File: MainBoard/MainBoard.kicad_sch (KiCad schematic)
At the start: 53 parts, among them J1 Conn_02x04_Odd_Even, SW1 DSHP02TSGET, U1 W25Q16JVUXIQ, U13 74LVC1G34GW,125, U14 SIP32431DR3-T1GE3, U2 RP2040, Y1 12.000MHz

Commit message: Move main PCB into subdirectory so that we can add a bezel PCB to this repo
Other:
- company: Framework Computer Inc -> C. Scott Ananian
- title: LED Matrix Input Module -> Seven Segment Display Input Module
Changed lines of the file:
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@@
 	(paper "A3")
 	(title_block
-		(title "LED Matrix Input Module")
-		(date "2022-12-18")
-		(company "Framework Computer Inc")
+		(title "Seven Segment Display Input Module")
+		(date "2024-07-13")
+		(company "C. Scott Ananian")
 		(comment 1 "This work is licensed under a Creative Commons Attribution 4.0 International License")
-		(comment 2 "https://github.com/FrameworkComputer/InputModules")
-		(comment 3 "https://frame.work")
+		(comment 2 "https://github.com/cscott/SevenSegmentInputModule")
+		(comment 3 "https://cscott.net")
 	)
 	(junction
@@
 		)
 		(instances
-			(project "SevenSegment"
+			(project "MainBoard"
 				(path "/2fa7b4ce-e682-4c2e-9419-b1318fe8c56d"
 					(page "2")

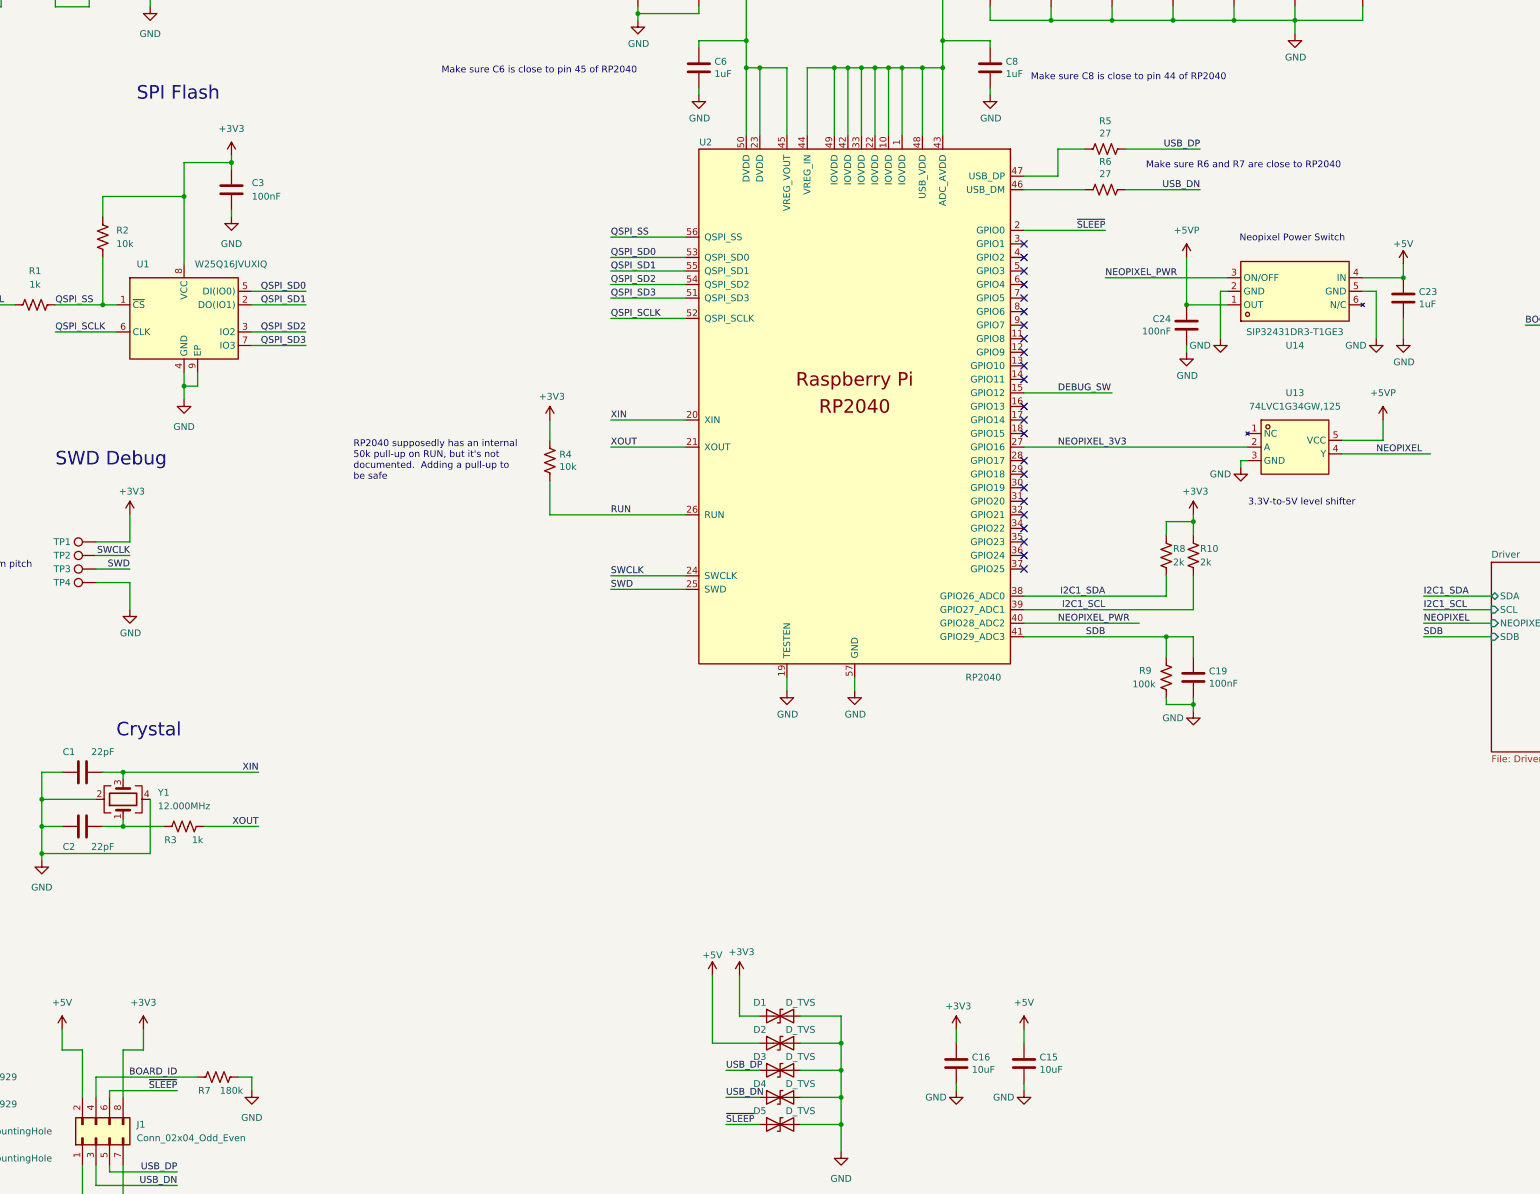
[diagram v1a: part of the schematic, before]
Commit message: Optimize for manufacturability (use JLCPCB basic parts, etc)
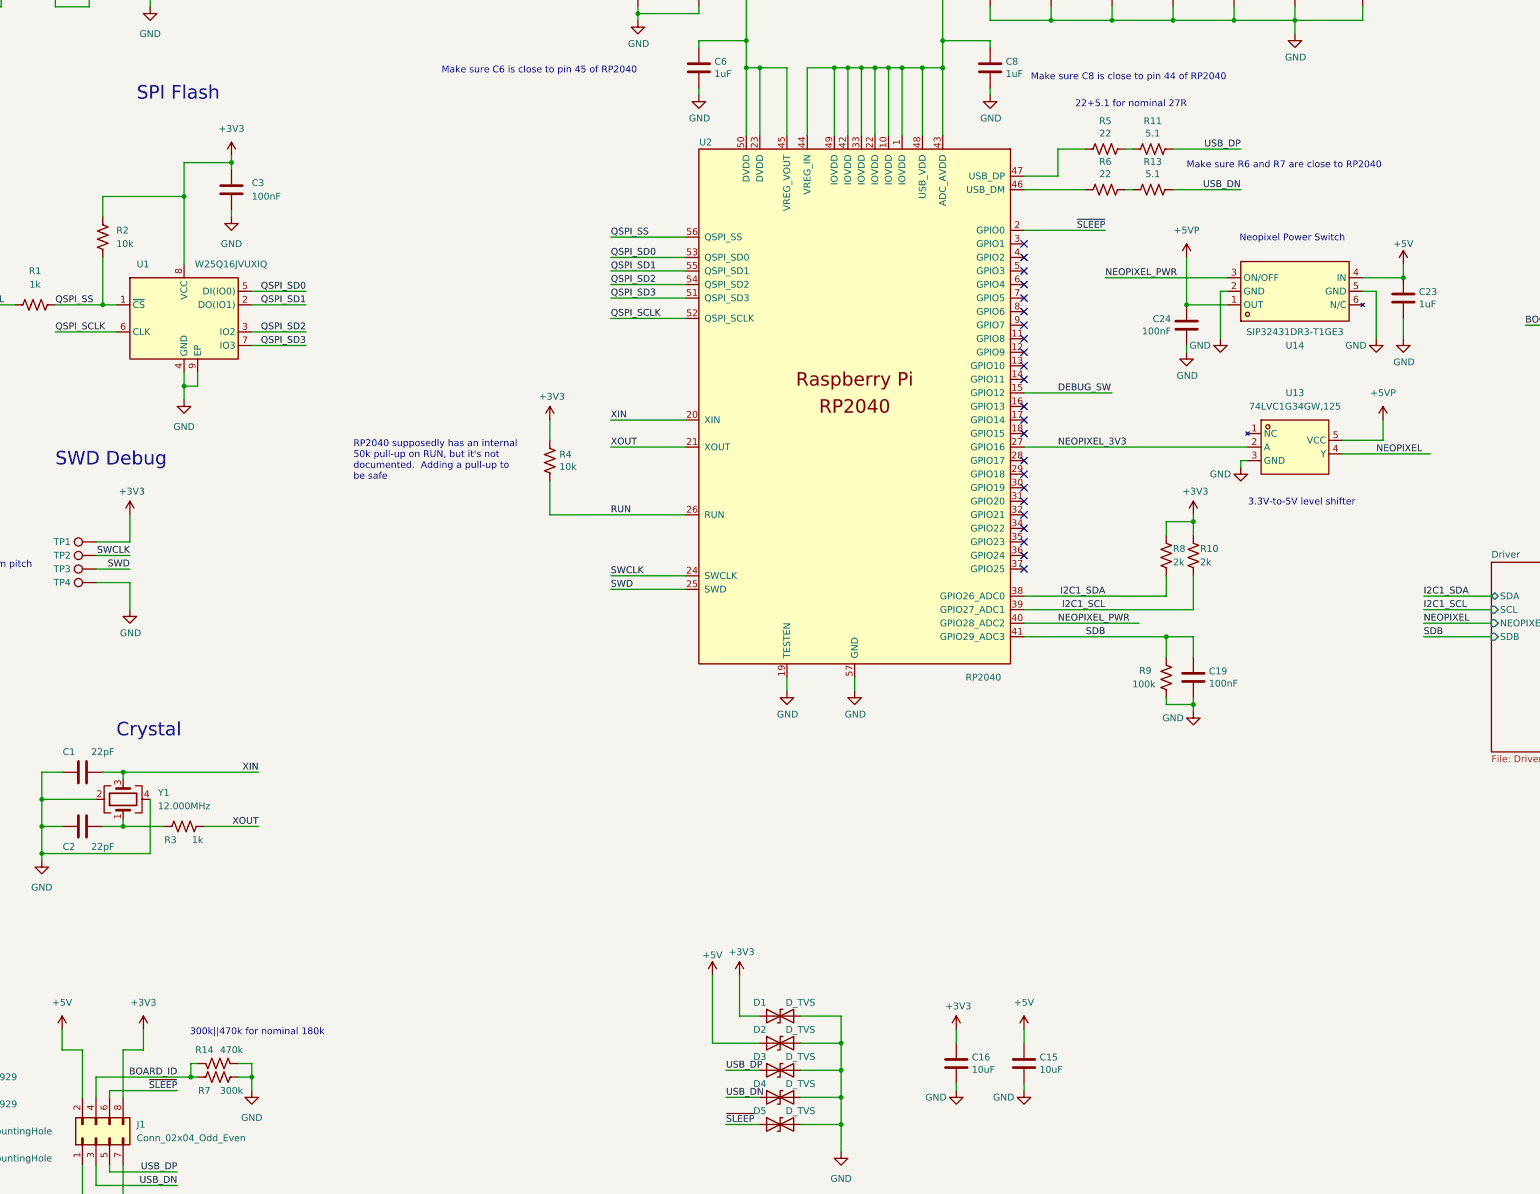
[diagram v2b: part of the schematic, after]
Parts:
- added R11, R13: 5.1, Resistor_SMD:R_0603_1608Metric, symbol Device:R_US
- added R14: 470k, Resistor_SMD:R_0603_1608Metric, symbol Device:R_US
- R5, R6: value 27 -> 22; Digikey P27.0LCT-ND -> P22.0LCT-ND; LCSC C138021 -> C25092
- R7: value 180k -> 300k; footprint Resistor_SMD:R_0402_1005Metric -> Resistor_SMD:R_0603_1608Metric; LCSC C25760 -> C23024
- U13, U14: JLCPCB Rotation Offset (none) -> 180
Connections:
- net BOARD_ID: now also R14.1
- net GND: now also R14.2
- net USB_DN: now also R13.1; no longer R6.1
- net USB_DP: now also R11.1; no longer R5.1
- new net: R11.2, R5.1
- new net: R13.2, R6.1
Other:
- note added: "22+5.1 for nominal 27R"
- note added: "300k||470k for nominal 180k"

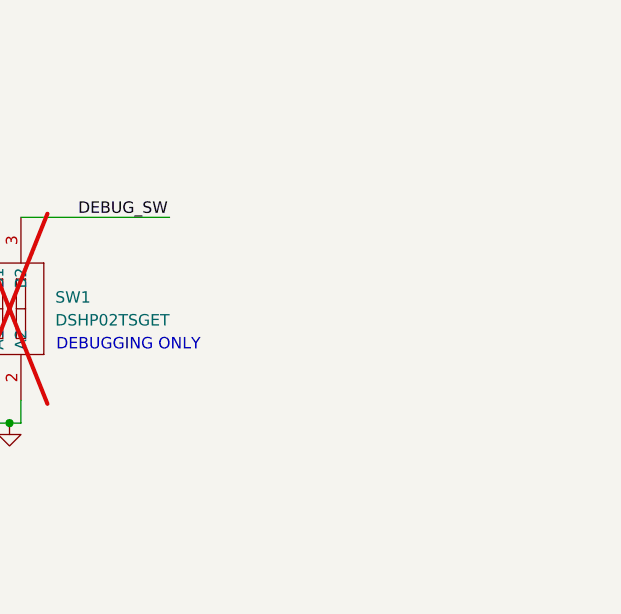
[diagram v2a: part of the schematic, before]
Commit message: Add neopixel debugging header
This allows us to fab just the neopixels on the board, saving some cost
while we check to see how the backlight looks.
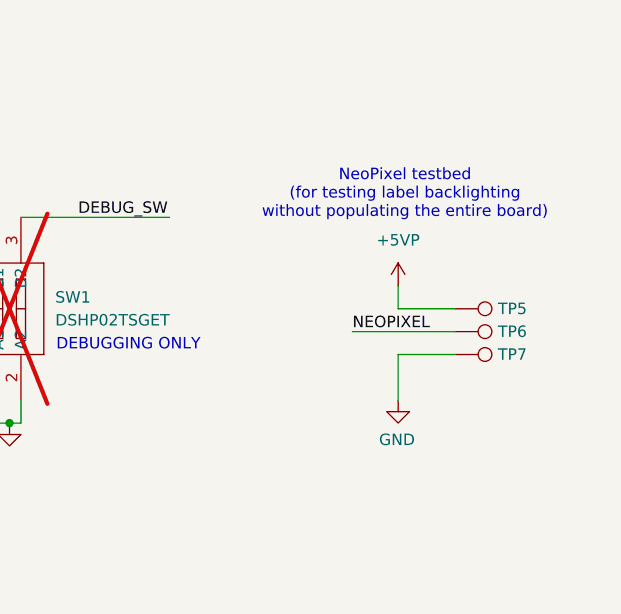
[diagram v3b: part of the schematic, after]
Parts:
- added TP5, TP6, TP7: TestPoint, TestPoint:TestPoint_Pad_D1.0mm, symbol Connector:TestPoint
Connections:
- net +5VP: now also TP5.1
- net GND: now also TP7.1
- net NEOPIXEL: now also TP6.1
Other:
- note added: "NeoPixel testbed (for testing label backlighting without populating the entire board)"

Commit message: Use 'dumb' 3.1V white LEDs instead of neopixels for legend backlighting
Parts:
- removed C15: 10uF, Capacitor_SMD:C_0603_1608Metric, symbol Device:C
- removed C23: 1uF, Capacitor_SMD:C_0402_1005Metric, symbol Device:C
- removed C24: 100nF, Capacitor_SMD:C_0402_1005Metric, symbol Device:C
- removed D2: D_TVS, Diode_SMD:D_0402_1005Metric, symbol Device:D_TVS
- removed TP5, TP6, TP7: TestPoint, TestPoint:TestPoint_Pad_D1.0mm, symbol Connector:TestPoint
- removed U13: 74LVC1G34GW,125, LCSC:SOT-353_L2.1-W1.3-P0.65-LS2.3-BR, symbol LCSC:74LVC1G34GW,125
- removed U14: SIP32431DR3-T1GE3, LCSC:SOT-363_L2.0-W1.3-P0.65-LS2.1-BR, symbol LCSC:SIP32431DR3-T1GE3
- U1: value W25Q16JVUXIQ -> W25Q16JVUXIQ
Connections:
- net +5V: no longer names the net of J1.2 (Pin_2)
- net NEOPIXEL_3V3: no longer names the net of U2.27 (GPIO16)
- net NEOPIXEL_PWR: no longer names the net of U2.40 (GPIO28_ADC2)
- no-connect marks 23 -> 26
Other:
- sheet Driver ports: added none; removed NEOPIXEL
- note removed: "3.3V-to-5V level shifter"
- note removed: "NeoPixel testbed (for testing label backlighting without populating the entire board)"
- note removed: "Neopixel Power Switch"
